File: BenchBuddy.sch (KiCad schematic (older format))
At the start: 0 parts

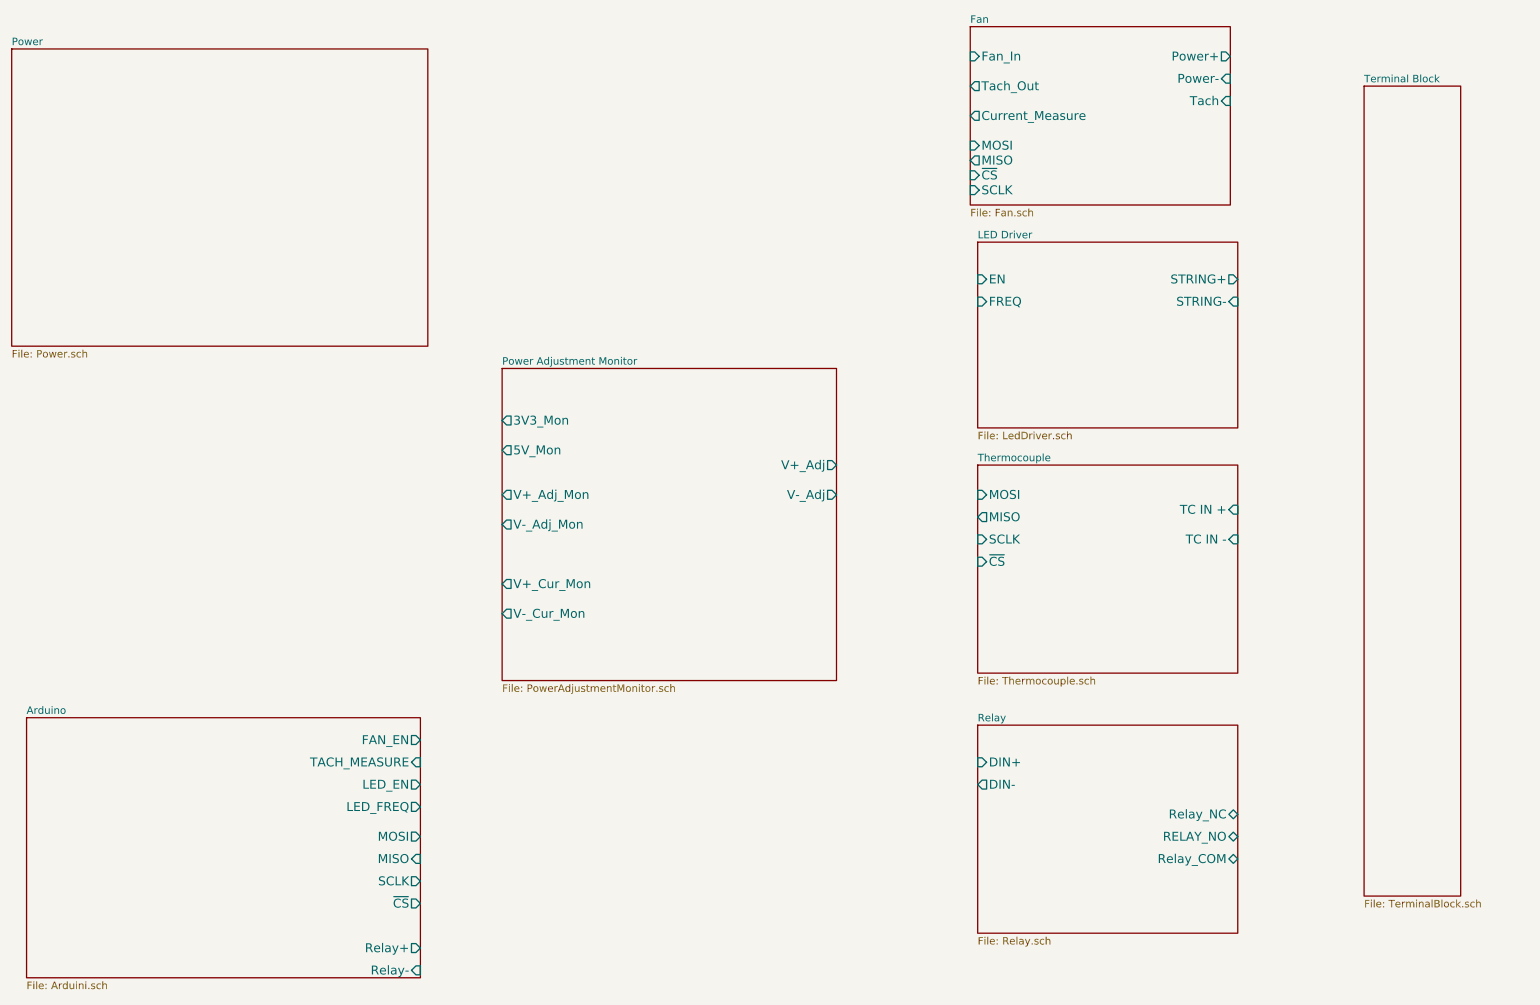
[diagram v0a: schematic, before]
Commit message: Added connections to Terminal Block
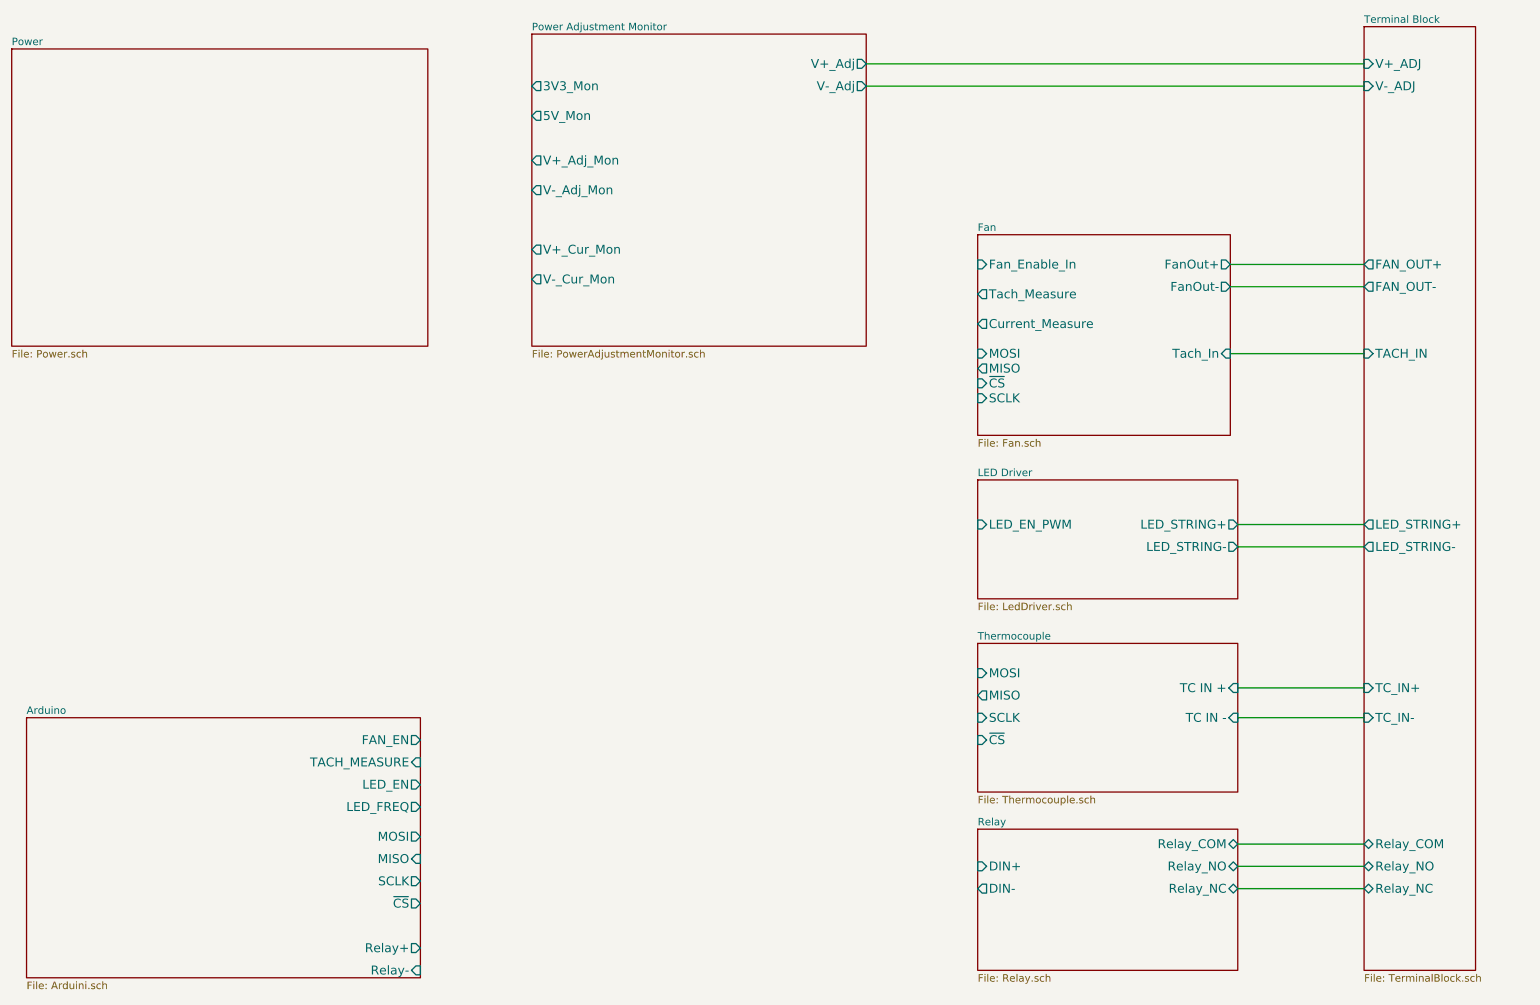
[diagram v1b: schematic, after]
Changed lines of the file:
@@
 $EndDescr
 $Sheet
-S 7650 3600 1750 1400
+S 7650 4800 1750 1000
 U 52326E49
 F0 "Thermocouple" 50
 F1 "Thermocouple.sch" 50
-F2 "TC IN +" I R 9400 3900 60
-F3 "TC IN -" I R 9400 4100 60
-F4 "MOSI" I L 7650 3800 60
-F5 "MISO" O L 7650 3950 60
-F6 "SCLK" I L 7650 4100 60
-F7 "~CS" I L 7650 4250 60
+F2 "TC IN +" I R 9400 5100 60
+F3 "TC IN -" I R 9400 5300 60
+F4 "MOSI" I L 7650 5000 60
+F5 "MISO" O L 7650 5150 60
+F6 "SCLK" I L 7650 5300 60
+F7 "~CS" I L 7650 5450 60
 $EndSheet
 $Sheet
-S 7650 5350 1750 1400
+S 7650 6050 1750 950
 U 52326E5C
 F0 "Relay" 50
 F1 "Relay.sch" 50
-F2 "DIN+" I L 7650 5600 60
-F3 "DIN-" O L 7650 5750 60
-F4 "Relay_NC" B R 9400 5950 60
-F5 "RELAY_NO" B R 9400 6100 60
-F6 "Relay_COM" B R 9400 6250 60
+F2 "DIN+" I L 7650 6300 60
+F3 "DIN-" O L 7650 6450 60
+F4 "Relay_NC" B R 9400 6450 60
+F5 "Relay_COM" B R 9400 6150 60
+F6 "Relay_NO" B R 9400 6300 60
 $EndSheet
 $Sheet
@@
 $EndSheet
 $Sheet
-S 7650 2100 1750 1250
-U 52326EDF
-F0 "LED Driver" 50
-F1 "LedDriver.sch" 50
-F2 "EN" I L 7650 2350 60
-F3 "FREQ" I L 7650 2500 60
-F4 "STRING+" O R 9400 2350 60
-F5 "STRING-" I R 9400 2500 60
-$EndSheet
-$Sheet
-S 7600 650  1750 1200
+S 7650 2050 1700 1350
 U 52326F15
 F0 "Fan" 50
 F1 "Fan.sch" 50
-F2 "Power+" O R 9350 850 60
-F3 "Power-" I R 9350 1000 60
-F4 "Tach" I R 9350 1150 60
-F5 "Tach_Out" O L 7600 1050 60
-F6 "Fan_In" I L 7600 850 60
-F7 "Current_Measure" O L 7600 1250 60
-F8 "MOSI" I L 7600 1450 60
-F9 "MISO" O L 7600 1550 60
-F10 "~CS" I L 7600 1650 60
-F11 "SCLK" I L 7600 1750 60
-$EndSheet
-$Sheet
-S 10250 1050 650  5450
-U 52326F21
-F0 "Terminal Block" 50
-F1 "TerminalBlock.sch" 50
+F2 "Current_Measure" O L 7650 2650 60
+F3 "MOSI" I L 7650 2850 60
+F4 "MISO" O L 7650 2950 60
+F5 "~CS" I L 7650 3050 60
+F6 "SCLK" I L 7650 3150 60
+F7 "FanOut+" O R 9350 2250 60
+F8 "Tach_In" I R 9350 2850 60
+F9 "Tach_Measure" O L 7650 2450 60
+F10 "Fan_Enable_In" I L 7650 2250 60
+F11 "FanOut-" O R 9350 2400 60
 $EndSheet
 $Sheet
@@
 $EndSheet
 $Sheet
-S 4450 2950 2250 2100
+S 7650 3700 1750 800
+U 52326EDF
+F0 "LED Driver" 50
+F1 "LedDriver.sch" 50
+F2 "LED_EN_PWM" I L 7650 4000 60
+F3 "LED_STRING+" O R 9400 4000 60
+F4 "LED_STRING-" O R 9400 4150 60
+$EndSheet
+$Sheet
+S 10250 650  750  6350
+U 52326F21
+F0 "Terminal Block" 50
+F1 "TerminalBlock.sch" 50
+F2 "V+_ADJ" I L 10250 900 60
+F3 "V-_ADJ" I L 10250 1050 60
+F4 "FAN_OUT+" O L 10250 2250 60
+F5 "FAN_OUT-" O L 10250 2400 60
+F6 "TACH_IN" I L 10250 2850 60
+F7 "LED_STRING+" O L 10250 4000 60
+F8 "LED_STRING-" O L 10250 4150 60
+F9 "TC_IN+" I L 10250 5100 60
+F10 "TC_IN-" I L 10250 5300 60
+F11 "Relay_COM" B L 10250 6150 60
+F12 "Relay_NO" B L 10250 6300 60
+F13 "Relay_NC" B L 10250 6450 60
+$EndSheet
+Wire Wire Line
+	9400 6150 10250 6150
+Wire Wire Line
+	9400 6300 10250 6300
+Wire Wire Line
+	9400 6450 10250 6450
+Wire Wire Line
+	9400 5100 10250 5100
+Wire Wire Line
+	9400 5300 10250 5300
+Wire Wire Line
+	9400 4000 10250 4000
+Wire Wire Line
+	9400 4150 10250 4150
+Wire Wire Line
+	9350 2850 10250 2850
+Wire Wire Line
+	9350 2400 10250 2400
+Wire Wire Line
+	9350 2250 10250 2250
+$Sheet
+S 4650 700  2250 2100
 U 524E194C
 F0 "Power Adjustment Monitor" 50
 F1 "PowerAdjustmentMonitor.sch" 50
-F2 "3V3_Mon" O L 4450 3300 60
-F3 "5V_Mon" O L 4450 3500 60
-F4 "V+_Adj_Mon" O L 4450 3800 60
-F5 "V-_Adj_Mon" O L 4450 4000 60
-F6 "V-_Cur_Mon" O L 4450 4600 60
-F7 "V+_Adj" O R 6700 3600 60
-F8 "V+_Cur_Mon" O L 4450 4400 60
-F9 "V-_Adj" O R 6700 3800 60
+F2 "3V3_Mon" O L 4650 1050 60
+F3 "5V_Mon" O L 4650 1250 60
+F4 "V+_Adj_Mon" O L 4650 1550 60
+F5 "V-_Adj_Mon" O L 4650 1750 60
+F6 "V-_Cur_Mon" O L 4650 2350 60
+F7 "V+_Adj" O R 6900 900 60
+F8 "V+_Cur_Mon" O L 4650 2150 60
+F9 "V-_Adj" O R 6900 1050 60
 $EndSheet
+Wire Wire Line
+	6900 900  10250 900
+Wire Wire Line
+	6900 1050 10250 1050
 $EndSCHEMATC

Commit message: Arduino Module Connection
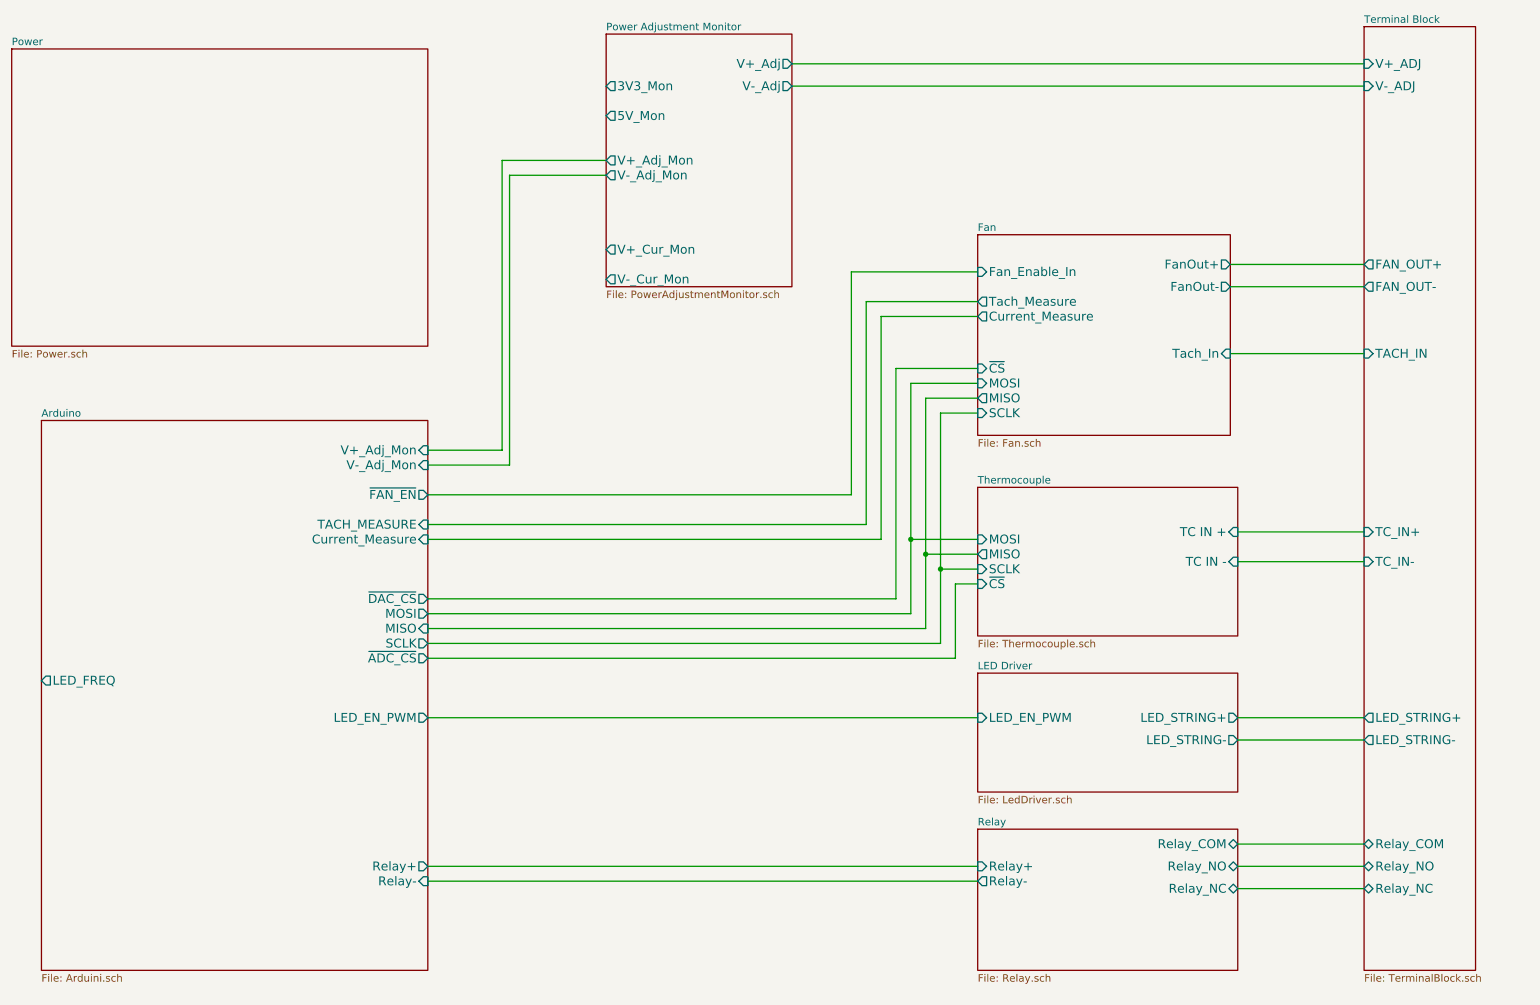
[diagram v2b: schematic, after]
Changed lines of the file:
@@
 Sheet 1 9
 Title ""
-Date "11 oct 2013"
+Date "22 oct 2013"
 Rev ""
 Comp ""
@@
 $EndDescr
 $Sheet
-S 7650 4800 1750 1000
+S 7650 3750 1750 1000
 U 52326E49
 F0 "Thermocouple" 50
 F1 "Thermocouple.sch" 50
-F2 "TC IN +" I R 9400 5100 60
-F3 "TC IN -" I R 9400 5300 60
-F4 "MOSI" I L 7650 5000 60
-F5 "MISO" O L 7650 5150 60
-F6 "SCLK" I L 7650 5300 60
-F7 "~CS" I L 7650 5450 60
+F2 "TC IN +" I R 9400 4050 60
+F3 "TC IN -" I R 9400 4250 60
+F4 "MOSI" I L 7650 4100 60
+F5 "MISO" O L 7650 4200 60
+F6 "SCLK" I L 7650 4300 60
+F7 "~CS" I L 7650 4400 60
 $EndSheet
 $Sheet
@@
 F0 "Relay" 50
 F1 "Relay.sch" 50
-F2 "DIN+" I L 7650 6300 60
-F3 "DIN-" O L 7650 6450 60
-F4 "Relay_NC" B R 9400 6450 60
-F5 "Relay_COM" B R 9400 6150 60
-F6 "Relay_NO" B R 9400 6300 60
+F2 "Relay_NC" B R 9400 6450 60
+F3 "Relay_COM" B R 9400 6150 60
+F4 "Relay_NO" B R 9400 6300 60
+F5 "Relay+" I L 7650 6300 60
+F6 "Relay-" O L 7650 6400 60
 $EndSheet
 $Sheet
@@
 F0 "Fan" 50
 F1 "Fan.sch" 50
-F2 "Current_Measure" O L 7650 2650 60
-F3 "MOSI" I L 7650 2850 60
-F4 "MISO" O L 7650 2950 60
-F5 "~CS" I L 7650 3050 60
-F6 "SCLK" I L 7650 3150 60
+F2 "Current_Measure" O L 7650 2600 60
+F3 "MOSI" I L 7650 3050 60
+F4 "MISO" O L 7650 3150 60
+F5 "~CS" I L 7650 2950 60
+F6 "SCLK" I L 7650 3250 60
 F7 "FanOut+" O R 9350 2250 60
 F8 "Tach_In" I R 9350 2850 60
-F9 "Tach_Measure" O L 7650 2450 60
-F10 "Fan_Enable_In" I L 7650 2250 60
+F9 "Tach_Measure" O L 7650 2500 60
+F10 "Fan_Enable_In" I L 7650 2300 60
 F11 "FanOut-" O R 9350 2400 60
 $EndSheet
 $Sheet
-S 1250 5300 2650 1750
+S 7650 5000 1750 800
+U 52326EDF
+F0 "LED Driver" 50
+F1 "LedDriver.sch" 50
+F2 "LED_EN_PWM" I L 7650 5300 60
+F3 "LED_STRING+" O R 9400 5300 60
+F4 "LED_STRING-" O R 9400 5450 60
+$EndSheet
+Wire Wire Line
+	9400 6150 10250 6150
+Wire Wire Line
+	9400 6300 10250 6300
+Wire Wire Line
+	9400 6450 10250 6450
+Wire Wire Line
+	9350 2850 10250 2850
+Wire Wire Line
+	9350 2400 10250 2400
+Wire Wire Line
+	9350 2250 10250 2250
+$Sheet
+S 5150 700  1250 1700
+U 524E194C
+F0 "Power Adjustment Monitor" 50
+F1 "PowerAdjustmentMonitor.sch" 50
+F2 "3V3_Mon" O L 5150 1050 60
+F3 "5V_Mon" O L 5150 1250 60
+F4 "V+_Adj_Mon" O L 5150 1550 60
+F5 "V-_Adj_Mon" O L 5150 1650 60
+F6 "V-_Cur_Mon" O L 5150 2350 60
+F7 "V+_Adj" O R 6400 900 60
+F8 "V+_Cur_Mon" O L 5150 2150 60
+F9 "V-_Adj" O R 6400 1050 60
+$EndSheet
+Wire Wire Line
+	6400 900  10250 900
+Wire Wire Line
+	6400 1050 10250 1050
+Wire Wire Line
+	5150 1550 4450 1550
+Wire Wire Line
+	4450 1550 4450 3500
+Wire Wire Line
+	4450 3500 3950 3500
+Wire Wire Line
+	5150 1650 4500 1650
+Wire Wire Line
+	4500 1650 4500 3600
+Wire Wire Line
+	4500 3600 3950 3600
+Wire Wire Line
+	7400 3250 7400 4800
+Connection ~ 7400 4300
+Wire Wire Line
+	7300 3150 7300 4700
+Connection ~ 7300 4200
+Wire Wire Line
+	7200 3050 7200 4600
+Connection ~ 7200 4100
+Wire Wire Line
+	7650 3250 7400 3250
+Wire Wire Line
+	7650 3150 7300 3150
+Wire Wire Line
+	7650 3050 7200 3050
+Wire Wire Line
+	7650 2950 7100 2950
+Wire Wire Line
+	7100 2950 7100 4500
+Wire Wire Line
+	7650 5300 3950 5300
+Wire Wire Line
+	7650 6300 3950 6300
+Wire Wire Line
+	3950 6400 7650 6400
+Wire Wire Line
+	7100 4500 3950 4500
+Wire Wire Line
+	7200 4600 3950 4600
+Wire Wire Line
+	7650 4100 7200 4100
+Wire Wire Line
+	7300 4200 7650 4200
+Wire Wire Line
+	7300 4700 3950 4700
+Wire Wire Line
+	7400 4300 7650 4300
+Wire Wire Line
+	7400 4800 3950 4800
+Wire Wire Line
+	7650 4400 7500 4400
+Wire Wire Line
+	7500 4400 7500 4900
+Wire Wire Line
+	7500 4900 3950 4900
+$Sheet
+S 1350 3300 2600 3700
 U 52326DF6
 F0 "Arduino" 50
 F1 "Arduini.sch" 50
-F2 "Relay+" O R 3900 6850 60
-F3 "Relay-" I R 3900 7000 60
-F4 "MOSI" O R 3900 6100 60
-F5 "MISO" I R 3900 6250 60
-F6 "SCLK" O R 3900 6400 60
-F7 "~CS" O R 3900 6550 60
-F8 "LED_EN" O R 3900 5750 60
-F9 "LED_FREQ" O R 3900 5900 60
-F10 "FAN_EN" O R 3900 5450 60
-F11 "TACH_MEASURE" I R 3900 5600 60
-$EndSheet
-$Sheet
-S 7650 3700 1750 800
-U 52326EDF
-F0 "LED Driver" 50
-F1 "LedDriver.sch" 50
-F2 "LED_EN_PWM" I L 7650 4000 60
-F3 "LED_STRING+" O R 9400 4000 60
-F4 "LED_STRING-" O R 9400 4150 60
-$EndSheet
+F2 "Relay+" O R 3950 6300 60
+F3 "Relay-" I R 3950 6400 60
+F4 "MOSI" O R 3950 4600 60
+F5 "MISO" I R 3950 4700 60
+F6 "SCLK" O R 3950 4800 60
+F7 "LED_FREQ" O L 1350 5050 60
+F8 "TACH_MEASURE" I R 3950 4000 60
+F9 "~FAN_EN" O R 3950 3800 60
+F10 "Current_Measure" I R 3950 4100 60
+F11 "LED_EN_PWM" O R 3950 5300 60
+F12 "V+_Adj_Mon" I R 3950 3500 60
+F13 "V-_Adj_Mon" I R 3950 3600 60
+F14 "~DAC_CS" O R 3950 4500 60
+F15 "~ADC_CS" O R 3950 4900 60
+$EndSheet
+Wire Wire Line
+	7650 2600 7000 2600
+Wire Wire Line
+	7000 2600 7000 4100
+Wire Wire Line
+	7000 4100 3950 4100
+Wire Wire Line
+	3950 4000 6900 4000
+Wire Wire Line
+	6900 4000 6900 2500
+Wire Wire Line
+	6900 2500 7650 2500
+Wire Wire Line
+	7650 2300 6800 2300
+Wire Wire Line
+	6800 2300 6800 3800
+Wire Wire Line
+	6800 3800 3950 3800
 $Sheet
 S 10250 650  750  6350
@@
 F5 "FAN_OUT-" O L 10250 2400 60
 F6 "TACH_IN" I L 10250 2850 60
-F7 "LED_STRING+" O L 10250 4000 60
-F8 "LED_STRING-" O L 10250 4150 60
-F9 "TC_IN+" I L 10250 5100 60
-F10 "TC_IN-" I L 10250 5300 60
+F7 "LED_STRING+" O L 10250 5300 60
+F8 "LED_STRING-" O L 10250 5450 60
+F9 "TC_IN+" I L 10250 4050 60
+F10 "TC_IN-" I L 10250 4250 60
 F11 "Relay_COM" B L 10250 6150 60
 F12 "Relay_NO" B L 10250 6300 60
@@
 $EndSheet
 Wire Wire Line
-	9400 6150 10250 6150
-Wire Wire Line
-	9400 6300 10250 6300
-Wire Wire Line
-	9400 6450 10250 6450
-Wire Wire Line
-	9400 5100 10250 5100
-Wire Wire Line
 	9400 5300 10250 5300
 Wire Wire Line
-	9400 4000 10250 4000
-Wire Wire Line
-	9400 4150 10250 4150
-Wire Wire Line
-	9350 2850 10250 2850
-Wire Wire Line
-	9350 2400 10250 2400
-Wire Wire Line
-	9350 2250 10250 2250
-$Sheet
-S 4650 700  2250 2100
-U 524E194C
-F0 "Power Adjustment Monitor" 50
-F1 "PowerAdjustmentMonitor.sch" 50
-F2 "3V3_Mon" O L 4650 1050 60
-F3 "5V_Mon" O L 4650 1250 60
-F4 "V+_Adj_Mon" O L 4650 1550 60
-F5 "V-_Adj_Mon" O L 4650 1750 60
-F6 "V-_Cur_Mon" O L 4650 2350 60
-F7 "V+_Adj" O R 6900 900 60
-F8 "V+_Cur_Mon" O L 4650 2150 60
-F9 "V-_Adj" O R 6900 1050 60
-$EndSheet
-Wire Wire Line
-	6900 900  10250 900
-Wire Wire Line
-	6900 1050 10250 1050
+	9400 5450 10250 5450
+Wire Wire Line
+	10250 4250 9400 4250
+Wire Wire Line
+	9400 4050 10250 4050
 $EndSCHEMATC
